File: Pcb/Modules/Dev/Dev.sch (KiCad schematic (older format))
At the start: 7 parts, among them J1 JACK_STEREO, J2 JACK_RJ45, P1 CONN_02X04, Q1 Q_NMOS_GSD, SW0 SW_TACTILE

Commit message: Fix missing wire on dev board and stop rounding corners on light pcb
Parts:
- R1: footprint (none) -> Resistors_SMD:R_0603
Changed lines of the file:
@@
 $EndComp
 $Comp
-L 3V3 #PWR3
+L 3V3 #PWR01
 U 1 1 58C31841
 P 2500 1150
-F 0 "#PWR3" H 2500 1250 40  0001 C CNN
+F 0 "#PWR01" H 2500 1250 40  0001 C CNN
 F 1 "3V3" H 2500 1275 40  0000 C CNN
 F 2 "" H 2500 1150 60  0000 C CNN
@@
 $EndComp
 $Comp
-L GND #PWR5
+L GND #PWR02
 U 1 1 58C3198F
 P 2650 1650
-F 0 "#PWR5" H 2650 1400 50  0001 C CNN
+F 0 "#PWR02" H 2650 1400 50  0001 C CNN
 F 1 "GND" H 2650 1500 50  0000 C CNN
 F 2 "" H 2650 1650 50  0000 C CNN
@@
 $EndComp
 $Comp
-L GND #PWR4
+L GND #PWR03
 U 1 1 58C31B87
 P 2500 2050
-F 0 "#PWR4" H 2500 1800 50  0001 C CNN
+F 0 "#PWR03" H 2500 1800 50  0001 C CNN
 F 1 "GND" H 2500 1900 50  0000 C CNN
 F 2 "" H 2500 2050 50  0000 C CNN
@@
 M_0
 $Comp
-L GND #PWR1
+L GND #PWR04
 U 1 1 58C32A9C
 P 1500 3000
-F 0 "#PWR1" H 1500 2750 50  0001 C CNN
+F 0 "#PWR04" H 1500 2750 50  0001 C CNN
 F 1 "GND" H 1500 2850 50  0000 C CNN
 F 2 "" H 1500 3000 50  0000 C CNN
@@
 NoConn ~ 2950 200
 $Comp
-L GND #PWR7
+L GND #PWR05
 U 1 1 58C34106
 P 3350 2250
-F 0 "#PWR7" H 3350 2000 50  0001 C CNN
+F 0 "#PWR05" H 3350 2000 50  0001 C CNN
 F 1 "GND" H 3350 2100 50  0000 C CNN
 F 2 "" H 3350 2250 50  0000 C CNN
@@
 $EndComp
 $Comp
-L 3V3 #PWR8
+L 3V3 #PWR06
 U 1 1 58C3412C
 P 4400 2250
-F 0 "#PWR8" H 4400 2350 40  0001 C CNN
+F 0 "#PWR06" H 4400 2350 40  0001 C CNN
 F 1 "3V3" H 4400 2375 40  0000 C CNN
 F 2 "" H 4400 2250 60  0000 C CNN
@@
 M_1
 $Comp
-L GND #PWR6
+L GND #PWR07
 U 1 1 59DE6C39
 P 3050 3400
-F 0 "#PWR6" H 3050 3150 50  0001 C CNN
+F 0 "#PWR07" H 3050 3150 50  0001 C CNN
 F 1 "GND" H 3050 3250 50  0000 C CNN
 F 2 "" H 3050 3400 50  0000 C CNN
@@
 F 0 "R1" V 2630 3000 50  0000 C CNN
 F 1 "1K" V 2550 3000 50  0000 C CNN
-F 2 "" V 2480 3000 50  0000 C CNN
+F 2 "Resistors_SMD:R_0603" V 2480 3000 50  0001 C CNN
 F 3 "" H 2550 3000 50  0000 C CNN
 	1    2550 3000
@@
 $EndComp
 $Comp
-L 3V3 #PWR?
+L 3V3 #PWR08
 U 1 1 59E3F80E
 P 2250 3300
-F 0 "#PWR?" H 2250 3400 40  0001 C CNN
+F 0 "#PWR08" H 2250 3400 40  0001 C CNN
 F 1 "3V3" H 2250 3425 40  0000 C CNN
 F 2 "" H 2250 3300 60  0000 C CNN

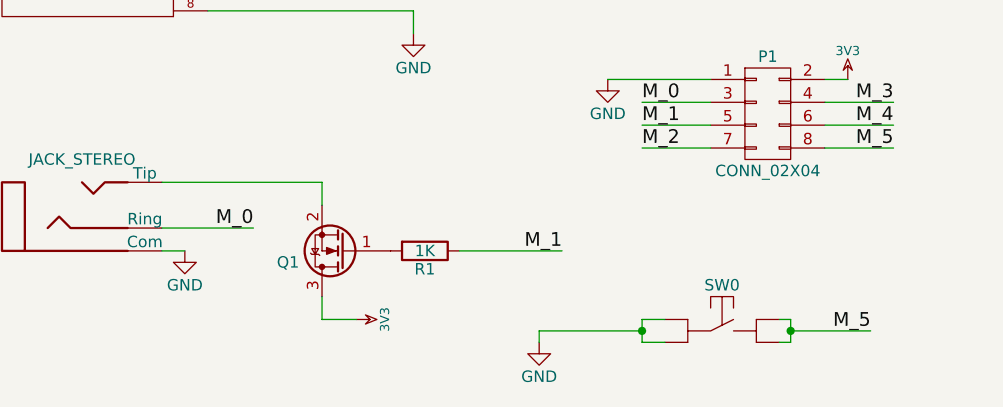
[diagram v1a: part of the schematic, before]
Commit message: Update module pcbs
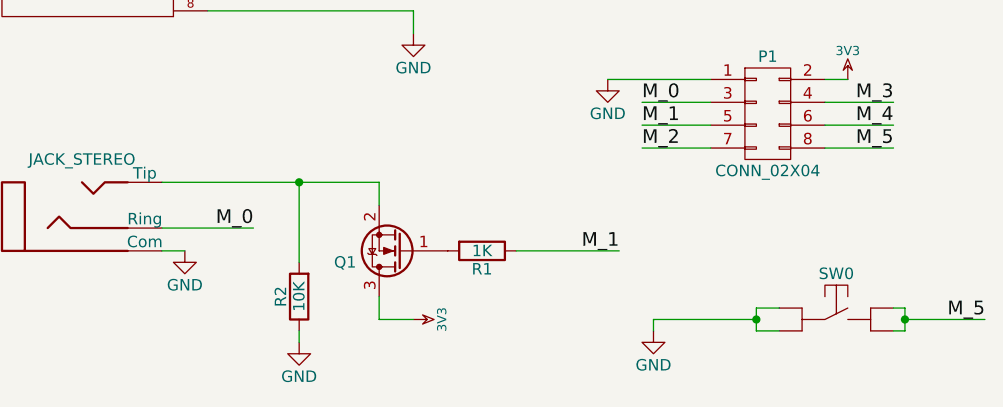
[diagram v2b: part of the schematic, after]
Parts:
- added R2: 10K, Resistors_SMD:R_0603, symbol R
- C1: value C -> 10uF
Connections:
- net GND: now also R2.1
- net at J1.2 (Tip), Q1.2 (S): now also R2.2
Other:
- moved on the sheet: Q1, R1, SW0
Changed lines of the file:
@@
 $EndComp
 Wire Wire Line
-	1400 2700 2100 2700
+	1400 2700 2350 2700
 Wire Wire Line
 	1400 2900 1800 2900
@@
 L Q_NMOS_GSD Q1
 U 1 1 59C1B522
-P 2200 3000
-F 0 "Q1" H 2400 3050 50  0000 L CNN
-F 1 "Q_NMOS_GSD" H 2400 2950 50  0001 L CNN
-F 2 "TO_SOT_Packages_SMD:SOT-23" H 2400 3100 50  0001 C CNN
-F 3 "" H 2200 3000 50  0000 C CNN
-	1    2200 3000
+P 2450 3000
+F 0 "Q1" H 2650 3050 50  0000 L CNN
+F 1 "Q_NMOS_GSD" H 2650 2950 50  0001 L CNN
+F 2 "TO_SOT_Packages_SMD:SOT-23" H 2650 3100 50  0001 C CNN
+F 3 "" H 2450 3000 50  0000 C CNN
+	1    2450 3000
 	-1   0    0    1
 $EndComp
@@
 L SW_TACTILE SW0
 U 1 1 59DE648C
-P 3850 3350
-F 0 "SW0" H 3850 3550 50  0000 C CNN
-F 1 "SW_TACTILE" H 3850 3250 50  0001 C CNN
-F 2 "CA6:PTS645" H 3850 3350 60  0001 C CNN
-F 3 "" H 3850 3350 60  0000 C CNN
-	1    3850 3350
-	1    0    0    -1
-$EndComp
-Wire Wire Line
-	3500 3300 3600 3300
-Wire Wire Line
-	3500 3400 3600 3400
-Wire Wire Line
-	4100 3300 4150 3300
-Wire Wire Line
-	4150 3300 4150 3400
-Wire Wire Line
-	4150 3350 4500 3350
-Wire Wire Line
-	4150 3400 4100 3400
-Connection ~ 4150 3350
-Wire Wire Line
-	2700 3000 3150 3000
-Wire Wire Line
-	3500 3300 3500 3400
-Wire Wire Line
-	3500 3350 3050 3350
-Connection ~ 3500 3350
-Text Label 3150 3000 2    60   ~ 0
+P 4350 3300
+F 0 "SW0" H 4350 3500 50  0000 C CNN
+F 1 "SW_TACTILE" H 4350 3200 50  0001 C CNN
+F 2 "CA6:PTS645" H 4350 3300 60  0001 C CNN
+F 3 "" H 4350 3300 60  0000 C CNN
+	1    4350 3300
+	1    0    0    -1
+$EndComp
+Wire Wire Line
+	4000 3250 4100 3250
+Wire Wire Line
+	4000 3350 4100 3350
+Wire Wire Line
+	4600 3250 4650 3250
+Wire Wire Line
+	4650 3250 4650 3350
+Wire Wire Line
+	4650 3300 5000 3300
+Wire Wire Line
+	4650 3350 4600 3350
+Connection ~ 4650 3300
+Wire Wire Line
+	2950 3000 3400 3000
+Wire Wire Line
+	4000 3250 4000 3350
+Wire Wire Line
+	4000 3300 3550 3300
+Connection ~ 4000 3300
+Text Label 3400 3000 2    60   ~ 0
 M_1
 $Comp
 L GND #PWR07
 U 1 1 59DE6C39
-P 3050 3400
-F 0 "#PWR07" H 3050 3150 50  0001 C CNN
-F 1 "GND" H 3050 3250 50  0000 C CNN
-F 2 "" H 3050 3400 50  0000 C CNN
-F 3 "" H 3050 3400 50  0000 C CNN
-	1    3050 3400
-	1    0    0    -1
-$EndComp
-Text Label 4500 3350 2    60   ~ 0
+P 3550 3350
+F 0 "#PWR07" H 3550 3100 50  0001 C CNN
+F 1 "GND" H 3550 3200 50  0000 C CNN
+F 2 "" H 3550 3350 50  0000 C CNN
+F 3 "" H 3550 3350 50  0000 C CNN
+	1    3550 3350
+	1    0    0    -1
+$EndComp
+Text Label 5000 3300 2    60   ~ 0
 M_5
 Wire Wire Line
-	3050 3350 3050 3400
+	3550 3300 3550 3350
 $Comp
 L C C1
@@
 P 2650 1400
 F 0 "C1" H 2675 1500 50  0000 L CNN
-F 1 "C" H 2675 1300 50  0001 L CNN
+F 1 "10uF" H 2675 1300 50  0001 L CNN
 F 2 "CA6:c_1206" H 2750 1300 50  0001 C CNN
 F 3 "" H 2650 1400 50  0000 C CNN
@@
 L R R1
 U 1 1 59E3F630
-P 2550 3000
-F 0 "R1" V 2630 3000 50  0000 C CNN
-F 1 "1K" V 2550 3000 50  0000 C CNN
-F 2 "Resistors_SMD:R_0603" V 2480 3000 50  0001 C CNN
-F 3 "" H 2550 3000 50  0000 C CNN
-	1    2550 3000
+P 2800 3000
+F 0 "R1" V 2880 3000 50  0000 C CNN
+F 1 "1K" V 2800 3000 50  0000 C CNN
+F 2 "Resistors_SMD:R_0603" V 2730 3000 50  0001 C CNN
+F 3 "" H 2800 3000 50  0000 C CNN
+	1    2800 3000
 	0    1    1    0
 $EndComp
@@
 L 3V3 #PWR08
 U 1 1 59E3F80E
-P 2250 3300
-F 0 "#PWR08" H 2250 3400 40  0001 C CNN
-F 1 "3V3" H 2250 3425 40  0000 C CNN
-F 2 "" H 2250 3300 60  0000 C CNN
-F 3 "" H 2250 3300 60  0000 C CNN
-	1    2250 3300
+P 2500 3300
+F 0 "#PWR08" H 2500 3400 40  0001 C CNN
+F 1 "3V3" H 2500 3425 40  0000 C CNN
+F 2 "" H 2500 3300 60  0000 C CNN
+F 3 "" H 2500 3300 60  0000 C CNN
+	1    2500 3300
 	0    1    1    0
 $EndComp
 Wire Wire Line
-	2250 3300 2100 3300
-Wire Wire Line
-	2100 3300 2100 3200
-Wire Wire Line
-	2100 2700 2100 2800
+	2500 3300 2350 3300
+Wire Wire Line
+	2350 3300 2350 3200
+Wire Wire Line
+	2350 2700 2350 2800
+$Comp
+L R R2
+U 1 1 5A21ED51
+P 2000 3200
+F 0 "R2" V 2080 3200 50  0000 C CNN
+F 1 "10K" V 2000 3200 50  0000 C CNN
+F 2 "Resistors_SMD:R_0603" V 1930 3200 50  0001 C CNN
+F 3 "" H 2000 3200 50  0000 C CNN
+	1    2000 3200
+	-1   0    0    1
+$EndComp
+Wire Wire Line
+	2000 3050 2000 2700
+Connection ~ 2000 2700
+$Comp
+L GND #PWR?
+U 1 1 5A21EDE2
+P 2000 3400
+F 0 "#PWR?" H 2000 3150 50  0001 C CNN
+F 1 "GND" H 2000 3250 50  0000 C CNN
+F 2 "" H 2000 3400 50  0000 C CNN
+F 3 "" H 2000 3400 50  0000 C CNN
+	1    2000 3400
+	1    0    0    -1
+$EndComp
+Wire Wire Line
+	2000 3350 2000 3400
 $EndSCHEMATC

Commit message: Update PCBs
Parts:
- added X1, X2, X3, X4: HOLE, Mounting_Holes:MountingHole_2.5mm_Pad, symbol HOLE
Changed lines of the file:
@@
 Connection ~ 2000 2700
 $Comp
-L GND #PWR?
+L GND #PWR09
 U 1 1 5A21EDE2
 P 2000 3400
-F 0 "#PWR?" H 2000 3150 50  0001 C CNN
+F 0 "#PWR09" H 2000 3150 50  0001 C CNN
 F 1 "GND" H 2000 3250 50  0000 C CNN
 F 2 "" H 2000 3400 50  0000 C CNN
@@
 Wire Wire Line
 	2000 3350 2000 3400
+$Comp
+L HOLE X1
+U 1 1 5A2341D5
+P 1650 4000
+F 0 "X1" H 1650 3900 60  0000 C CNN
+F 1 "HOLE" H 1650 4100 60  0000 C CNN
+F 2 "Mounting_Holes:MountingHole_2.5mm_Pad" H 1650 4000 60  0001 C CNN
+F 3 "" H 1650 4000 60  0000 C CNN
+	1    1650 4000
+	1    0    0    -1
+$EndComp
+$Comp
+L HOLE X2
+U 1 1 5A2343A7
+P 1950 4000
+F 0 "X2" H 1950 3900 60  0000 C CNN
+F 1 "HOLE" H 1950 4100 60  0000 C CNN
+F 2 "Mounting_Holes:MountingHole_2.5mm_Pad" H 1950 4000 60  0001 C CNN
+F 3 "" H 1950 4000 60  0000 C CNN
+	1    1950 4000
+	1    0    0    -1
+$EndComp
+$Comp
+L HOLE X3
+U 1 1 5A2343E7
+P 2250 4000
+F 0 "X3" H 2250 3900 60  0000 C CNN
+F 1 "HOLE" H 2250 4100 60  0000 C CNN
+F 2 "Mounting_Holes:MountingHole_2.5mm_Pad" H 2250 4000 60  0001 C CNN
+F 3 "" H 2250 4000 60  0000 C CNN
+	1    2250 4000
+	1    0    0    -1
+$EndComp
+$Comp
+L HOLE X4
+U 1 1 5A234424
+P 2550 4000
+F 0 "X4" H 2550 3900 60  0000 C CNN
+F 1 "HOLE" H 2550 4100 60  0000 C CNN
+F 2 "Mounting_Holes:MountingHole_2.5mm_Pad" H 2550 4000 60  0001 C CNN
+F 3 "" H 2550 4000 60  0000 C CNN
+	1    2550 4000
+	1    0    0    -1
+$EndComp
 $EndSCHEMATC

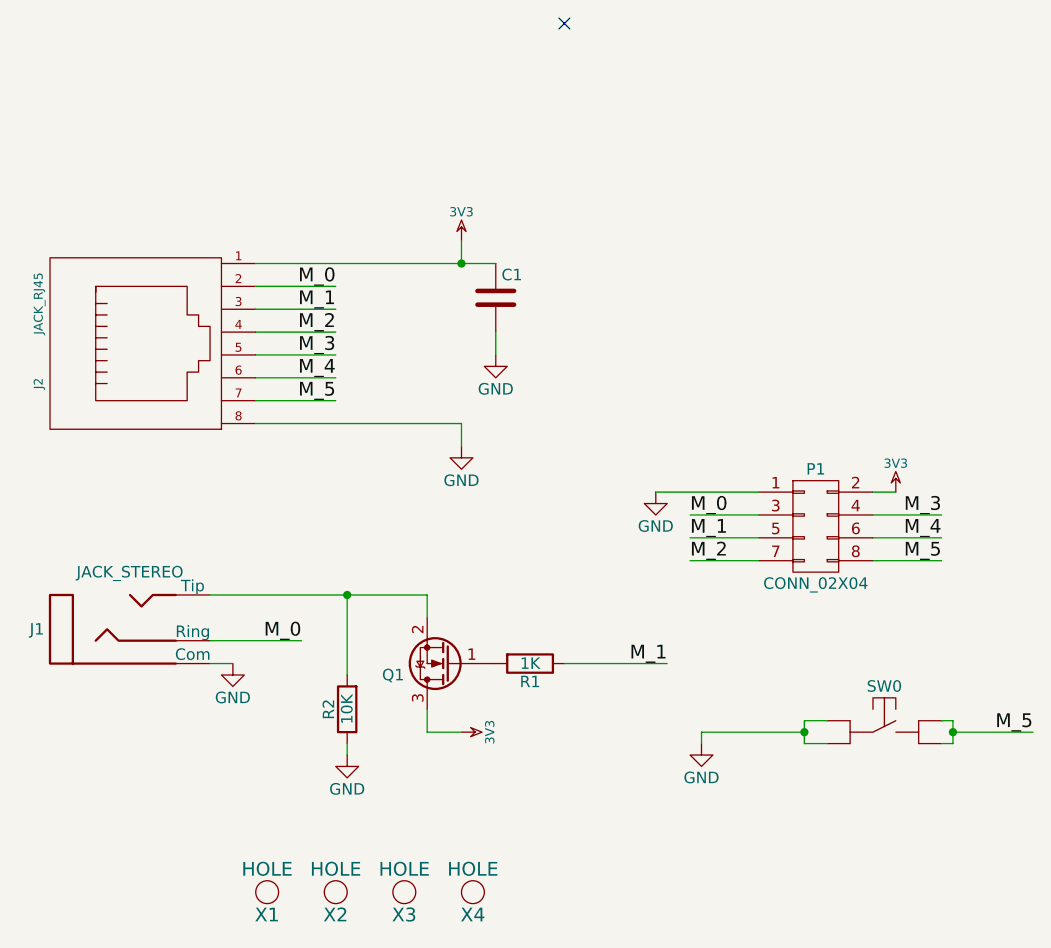
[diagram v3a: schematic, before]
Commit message: Update PCBs to use n channel mosfet on low side
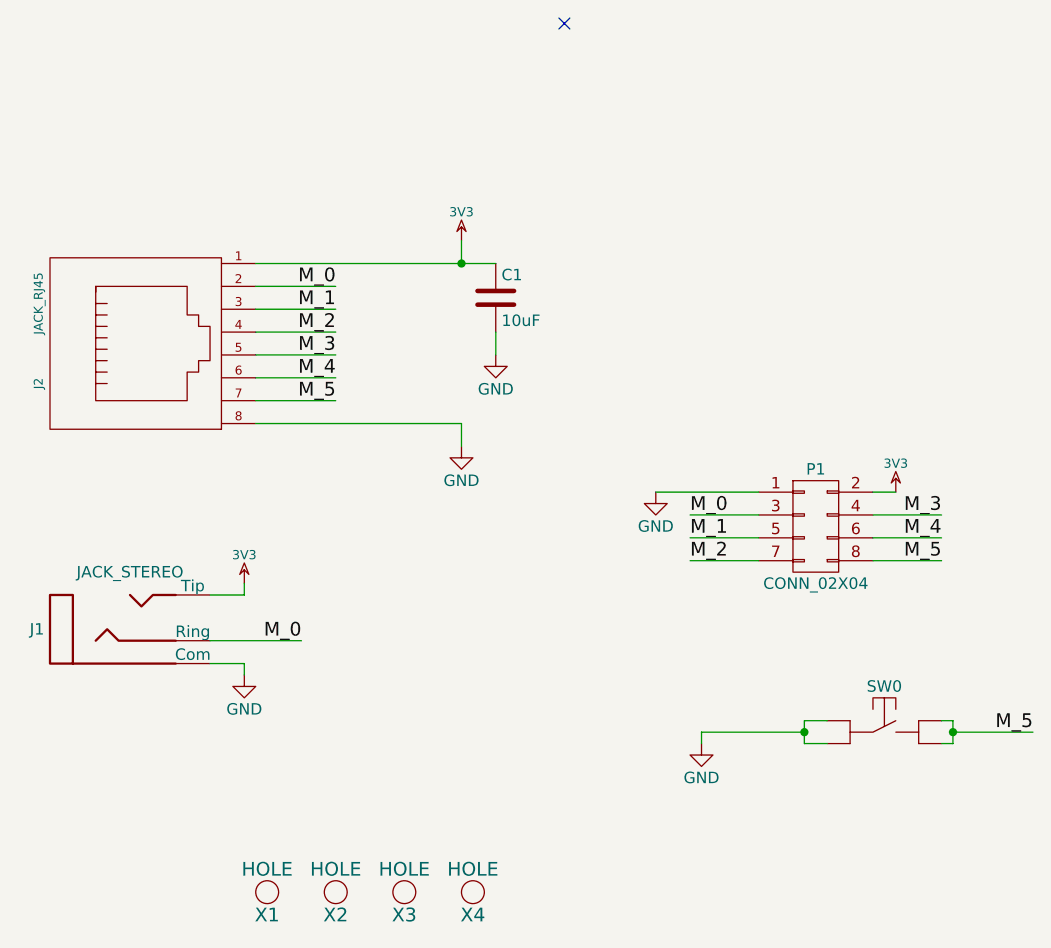
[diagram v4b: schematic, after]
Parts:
- removed Q1: Q_NMOS_GSD, TO_SOT_Packages_SMD:SOT-23, symbol Q_NMOS_GSD
- removed R1: 1K, Resistors_SMD:R_0603, symbol R
- removed R2: 10K, Resistors_SMD:R_0603, symbol R
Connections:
- net 3V3: now also J1.2 (Tip)
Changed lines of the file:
@@
 $EndComp
-Wire Wire Line
-	1400 2700 2350 2700
 Wire Wire Line
 	1400 2900 1800 2900
 Text Label 1800 2900 2    60   ~ 0
 M_0
+NoConn ~ 2950 200
 $Comp
 L GND #PWR04
-U 1 1 58C32A9C
-P 1500 3000
-F 0 "#PWR04" H 1500 2750 50  0001 C CNN
-F 1 "GND" H 1500 2850 50  0000 C CNN
-F 2 "" H 1500 3000 50  0000 C CNN
-F 3 "" H 1500 3000 50  0000 C CNN
-	1    1500 3000
-	1    0    0    -1
-$EndComp
-Wire Wire Line
-	1400 3000 1500 3000
-NoConn ~ 2950 200
-$Comp
-L GND #PWR05
 U 1 1 58C34106
 P 3350 2250
-F 0 "#PWR05" H 3350 2000 50  0001 C CNN
+F 0 "#PWR04" H 3350 2000 50  0001 C CNN
 F 1 "GND" H 3350 2100 50  0000 C CNN
 F 2 "" H 3350 2250 50  0000 C CNN
@@
 $EndComp
 $Comp
-L 3V3 #PWR06
+L 3V3 #PWR05
 U 1 1 58C3412C
 P 4400 2250
-F 0 "#PWR06" H 4400 2350 40  0001 C CNN
+F 0 "#PWR05" H 4400 2350 40  0001 C CNN
 F 1 "3V3" H 4400 2375 40  0000 C CNN
 F 2 "" H 4400 2250 60  0000 C CNN
@@
 	2500 1950 2500 2050
 $Comp
-L Q_NMOS_GSD Q1
-U 1 1 59C1B522
-P 2450 3000
-F 0 "Q1" H 2650 3050 50  0000 L CNN
-F 1 "Q_NMOS_GSD" H 2650 2950 50  0001 L CNN
-F 2 "TO_SOT_Packages_SMD:SOT-23" H 2650 3100 50  0001 C CNN
-F 3 "" H 2450 3000 50  0000 C CNN
-	1    2450 3000
-	-1   0    0    1
-$EndComp
-$Comp
 L SW_TACTILE SW0
 U 1 1 59DE648C
@@
 Connection ~ 4650 3300
 Wire Wire Line
-	2950 3000 3400 3000
-Wire Wire Line
 	4000 3250 4000 3350
 Wire Wire Line
 	4000 3300 3550 3300
 Connection ~ 4000 3300
-Text Label 3400 3000 2    60   ~ 0
-M_1
 $Comp
-L GND #PWR07
+L GND #PWR06
 U 1 1 59DE6C39
 P 3550 3350
-F 0 "#PWR07" H 3550 3100 50  0001 C CNN
+F 0 "#PWR06" H 3550 3100 50  0001 C CNN
 F 1 "GND" H 3550 3200 50  0000 C CNN
 F 2 "" H 3550 3350 50  0000 C CNN
@@
 P 2650 1400
 F 0 "C1" H 2675 1500 50  0000 L CNN
-F 1 "10uF" H 2675 1300 50  0001 L CNN
+F 1 "10uF" H 2675 1300 50  0000 L CNN
 F 2 "CA6:c_1206" H 2750 1300 50  0001 C CNN
 F 3 "" H 2650 1400 50  0000 C CNN
@@
 	1    0    0    -1
 $EndComp
-$Comp
-L R R1
-U 1 1 59E3F630
-P 2800 3000
-F 0 "R1" V 2880 3000 50  0000 C CNN
-F 1 "1K" V 2800 3000 50  0000 C CNN
-F 2 "Resistors_SMD:R_0603" V 2730 3000 50  0001 C CNN
-F 3 "" H 2800 3000 50  0000 C CNN
-	1    2800 3000
-	0    1    1    0
-$EndComp
-$Comp
-L 3V3 #PWR08
-U 1 1 59E3F80E
-P 2500 3300
-F 0 "#PWR08" H 2500 3400 40  0001 C CNN
-F 1 "3V3" H 2500 3425 40  0000 C CNN
-F 2 "" H 2500 3300 60  0000 C CNN
-F 3 "" H 2500 3300 60  0000 C CNN
-	1    2500 3300
-	0    1    1    0
-$EndComp
-Wire Wire Line
-	2500 3300 2350 3300
-Wire Wire Line
-	2350 3300 2350 3200
-Wire Wire Line
-	2350 2700 2350 2800
-$Comp
-L R R2
-U 1 1 5A21ED51
-P 2000 3200
-F 0 "R2" V 2080 3200 50  0000 C CNN
-F 1 "10K" V 2000 3200 50  0000 C CNN
-F 2 "Resistors_SMD:R_0603" V 1930 3200 50  0001 C CNN
-F 3 "" H 2000 3200 50  0000 C CNN
-	1    2000 3200
-	-1   0    0    1
-$EndComp
-Wire Wire Line
-	2000 3050 2000 2700
-Connection ~ 2000 2700
-$Comp
-L GND #PWR09
-U 1 1 5A21EDE2
-P 2000 3400
-F 0 "#PWR09" H 2000 3150 50  0001 C CNN
-F 1 "GND" H 2000 3250 50  0000 C CNN
-F 2 "" H 2000 3400 50  0000 C CNN
-F 3 "" H 2000 3400 50  0000 C CNN
-	1    2000 3400
-	1    0    0    -1
-$EndComp
-Wire Wire Line
-	2000 3350 2000 3400
 $Comp
 L HOLE X1
@@
 	1    0    0    -1
 $EndComp
+$Comp
+L 3V3 #PWR07
+U 1 1 5A36DAE6
+P 1550 2650
+F 0 "#PWR07" H 1550 2750 40  0001 C CNN
+F 1 "3V3" H 1550 2775 40  0000 C CNN
+F 2 "" H 1550 2650 60  0000 C CNN
+F 3 "" H 1550 2650 60  0000 C CNN
+	1    1550 2650
+	1    0    0    -1
+$EndComp
+Wire Wire Line
+	1400 2700 1550 2700
+Wire Wire Line
+	1550 2700 1550 2650
+$Comp
+L GND #PWR08
+U 1 1 5A36E71D
+P 1550 3050
+F 0 "#PWR08" H 1550 2800 50  0001 C CNN
+F 1 "GND" H 1550 2900 50  0000 C CNN
+F 2 "" H 1550 3050 50  0000 C CNN
+F 3 "" H 1550 3050 50  0000 C CNN
+	1    1550 3050
+	1    0    0    -1
+$EndComp
+Wire Wire Line
+	1400 3000 1550 3000
+Wire Wire Line
+	1550 3000 1550 3050
 $EndSCHEMATC

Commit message: Update pcb for new switch
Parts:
- C1: symbol C -> Device:C
- J1: symbol JACK_STEREO -> CA6:JACK_STEREO
- J2: symbol JACK_RJ45 -> CA6:JACK_RJ45
- P1: symbol CONN_02X04 -> Dev-rescue:CONN_02X04
- SW0: symbol SW_TACTILE -> CA6:SW_TACTILE
- X1, X2, X3, X4: symbol HOLE -> CA6:HOLE
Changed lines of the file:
@@
-EESchema Schematic File Version 2
-LIBS:power
-LIBS:device
-LIBS:transistors
-LIBS:conn
-LIBS:linear
-LIBS:regul
-LIBS:74xx
-LIBS:cmos4000
-LIBS:adc-dac
-LIBS:memory
-LIBS:xilinx
-LIBS:microcontrollers
-LIBS:dsp
-LIBS:microchip
-LIBS:analog_switches
-LIBS:motorola
-LIBS:texas
-LIBS:intel
-LIBS:audio
-LIBS:interface
-LIBS:digital-audio
-LIBS:philips
-LIBS:display
-LIBS:cypress
-LIBS:siliconi
-LIBS:opto
-LIBS:atmel
-LIBS:contrib
-LIBS:valves
-LIBS:CA6
+EESchema Schematic File Version 4
 LIBS:Dev-cache
-EELAYER 25 0
+EELAYER 26 0
 EELAYER END
 $Descr A4 11693 8268
@@
 $EndDescr
 $Comp
-L JACK_RJ45 J2
+L CA6:JACK_RJ45 J2
 U 1 1 58C31719
 P 1150 1600
@@
 $EndComp
 $Comp
-L 3V3 #PWR01
+L CA6:3V3 #PWR01
 U 1 1 58C31841
 P 2500 1150
@@
 $EndComp
 $Comp
-L GND #PWR02
+L power:GND #PWR02
 U 1 1 58C3198F
 P 2650 1650
@@
 $EndComp
 $Comp
-L GND #PWR03
+L power:GND #PWR03
 U 1 1 58C31B87
 P 2500 2050
@@
 M_5
 $Comp
-L JACK_STEREO J1
+L CA6:JACK_STEREO J1
 U 1 1 58C32458
 P 1050 2850
@@
 $EndComp
 $Comp
-L CONN_02X04 P1
+L Dev-rescue:CONN_02X04 P1
 U 1 1 58C324F0
 P 4050 2400
@@
 NoConn ~ 2950 200
 $Comp
-L GND #PWR04
+L power:GND #PWR04
 U 1 1 58C34106
 P 3350 2250
@@
 $EndComp
 $Comp
-L 3V3 #PWR05
+L CA6:3V3 #PWR05
 U 1 1 58C3412C
 P 4400 2250
@@
 M_5
 Wire Wire Line
-	1600 1250 2650 1250
+	1600 1250 2500 1250
 Wire Wire Line
 	2500 1150 2500 1250
@@
 	2500 1950 2500 2050
 $Comp
-L SW_TACTILE SW0
+L CA6:SW_TACTILE SW0
 U 1 1 59DE648C
 P 4350 3300
@@
 	4600 3250 4650 3250
 Wire Wire Line
-	4650 3250 4650 3350
+	4650 3250 4650 3300
 Wire Wire Line
 	4650 3300 5000 3300
@@
 Connection ~ 4650 3300
 Wire Wire Line
-	4000 3250 4000 3350
+	4000 3250 4000 3300
 Wire Wire Line
 	4000 3300 3550 3300
 Connection ~ 4000 3300
 $Comp
-L GND #PWR06
+L power:GND #PWR06
 U 1 1 59DE6C39
 P 3550 3350
@@
 	3550 3300 3550 3350
 $Comp
-L C C1
+L Device:C C1
 U 1 1 58C3185F
 P 2650 1400
@@
 $EndComp
 $Comp
-L HOLE X1
+L CA6:HOLE X1
 U 1 1 5A2341D5
 P 1650 4000
@@
 $EndComp
 $Comp
-L HOLE X2
+L CA6:HOLE X2
 U 1 1 5A2343A7
 P 1950 4000
@@
 $EndComp
 $Comp
-L HOLE X3
+L CA6:HOLE X3
 U 1 1 5A2343E7
 P 2250 4000
@@
 $EndComp
 $Comp
-L HOLE X4
+L CA6:HOLE X4
 U 1 1 5A234424
 P 2550 4000
@@
 $EndComp
 $Comp
-L 3V3 #PWR07
+L CA6:3V3 #PWR07
 U 1 1 5A36DAE6
 P 1550 2650
@@
 	1550 2700 1550 2650
 $Comp
-L GND #PWR08
+L power:GND #PWR08
 U 1 1 5A36E71D
 P 1550 3050
@@
 Wire Wire Line
 	1550 3000 1550 3050
+Wire Wire Line
+	2500 1250 2650 1250
+Wire Wire Line
+	4650 3300 4650 3350
+Wire Wire Line
+	4000 3300 4000 3350
 $EndSCHEMATC
